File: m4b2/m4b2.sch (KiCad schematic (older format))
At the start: 40 parts, among them P10 MicroD-37Pins, U1 MC306, U10 MC308, U11 MC306, U12 MC311, U13 MC309, U14 MC306, U15 MC308, U16 MC306, U17 MC311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

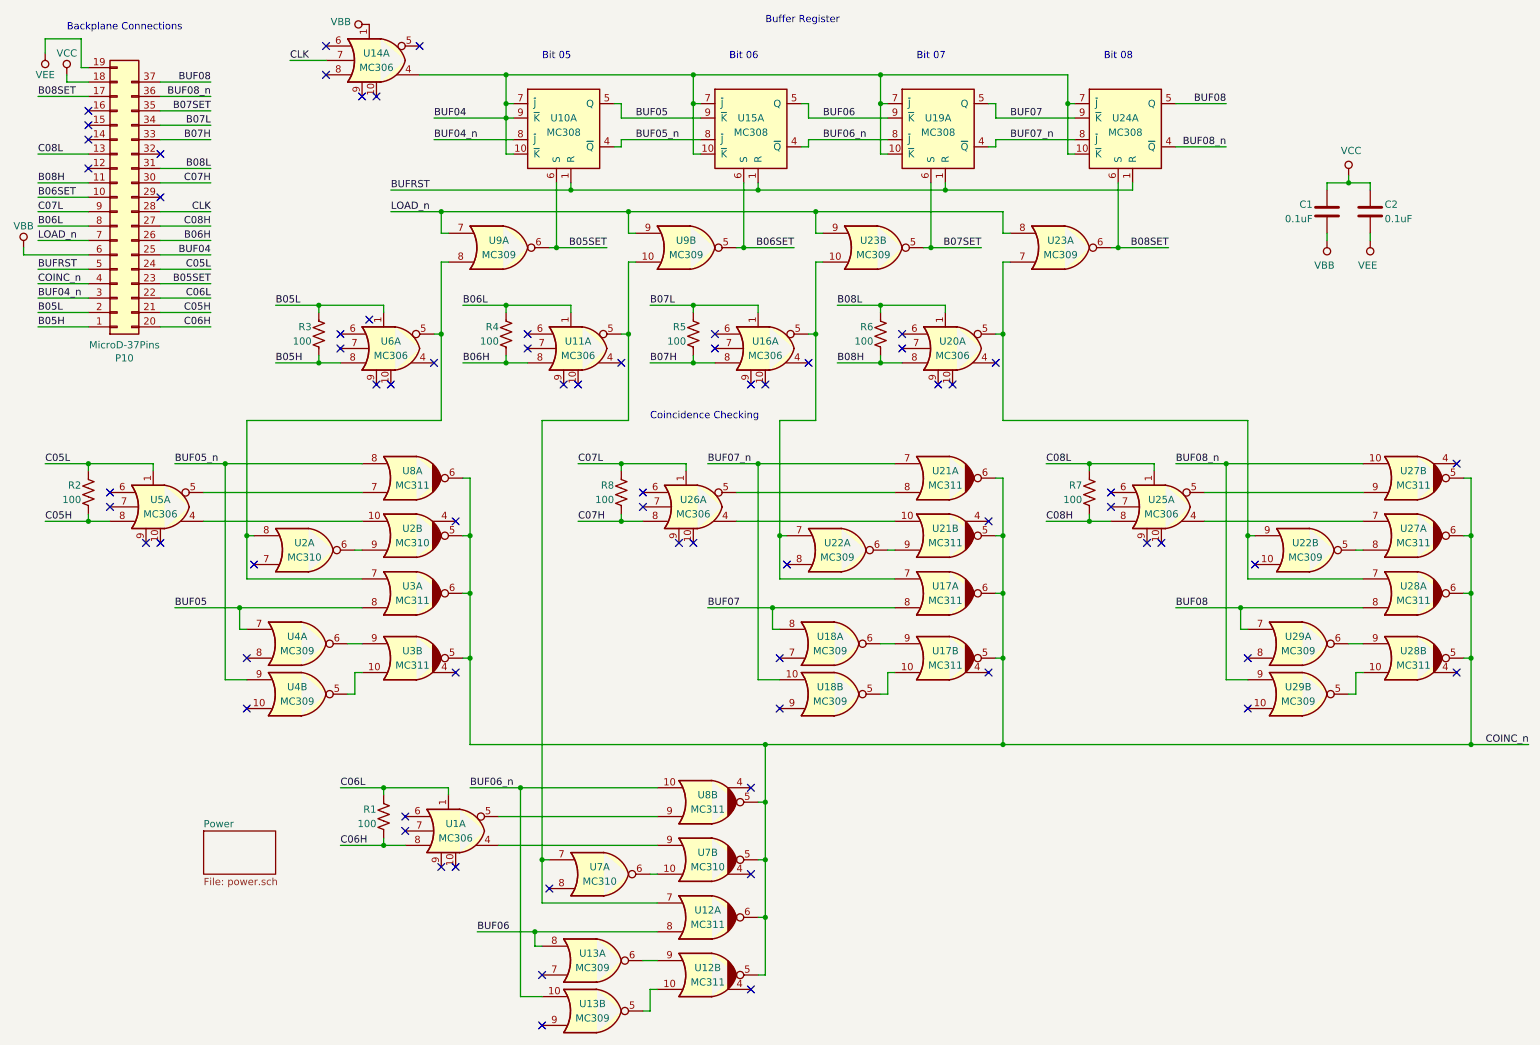
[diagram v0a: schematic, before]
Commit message: Added a schematic for module 4 board 2, which has two small differences from the other three four-bit modules. Also fixed a pinout error on module 5 board 2.
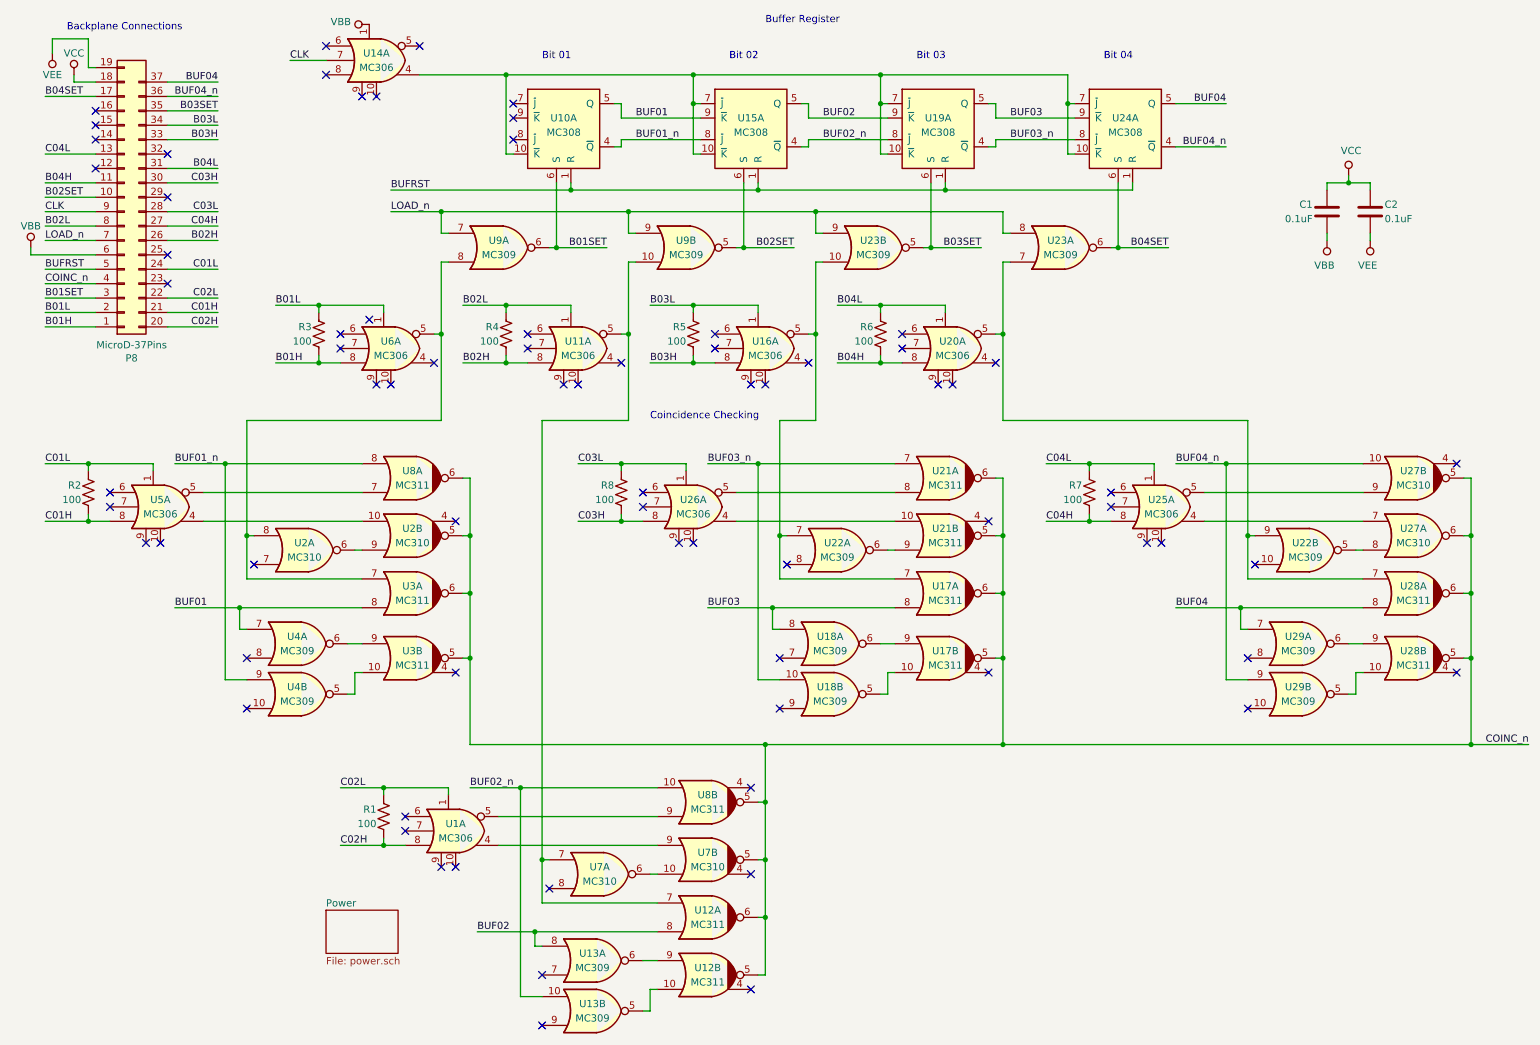
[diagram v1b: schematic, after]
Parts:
- removed P10: MicroD-37Pins, symbol gn_buffer:MicroD-37Pins
- removed U27: MC311, symbol gn_buffer:MC311
- added P8: MicroD-37Pins, symbol gn_buffer:MicroD-37Pins
- added U27: MC310, symbol gn_buffer:MC310
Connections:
- net BUF08 is gone; now on net BUF04: U24.5 (Q), U28.8, U29.7
- net BUF08_n is gone; now on net BUF04_n: U24.4 (~Q), U29.9
- net BUF04: now also P8.37 (Pin_37); no longer U10.10 (~K), U10.7 (~J), U10.9 (~K), U14.4, U15.10 (~K), U15.7 (~J), U19.10 (~K), U19.7 (~J), U24.10 (~K), U24.7 (~J)
- net BUF04_n: now also P8.36 (Pin_36), U27.10; no longer U10.8 (~J)
- net BUFRST: now also P8.5 (Pin_5)
- net CLK: now also P8.9 (Pin_9)
- net COINC_n: now also P8.4 (Pin_4), U27.5, U27.6
- net LOAD_n: now also P8.7 (Pin_7)
- net VBB: now also P8.6 (Pin_6)
- net VCC: now also P8.18 (Pin_18)
- net VEE: now also P8.19 (Pin_19)
- net at U25.4: now also U27.7
- net at U25.5: now also U27.9
- net at U22.5: now also U27.8
- net B05H renamed B01H
- net B01H: now also P8.1 (Pin_1)
- net B05L renamed B01L
- net B01L: now also P8.2 (Pin_2)
- net B05SET renamed B01SET
- net B01SET: now also P8.3 (Pin_3)
- net B06H renamed B02H
- net B02H: now also P8.26 (Pin_26)
- net B06L renamed B02L
- net B02L: now also P8.8 (Pin_8)
- net B06SET renamed B02SET
- net B02SET: now also P8.10 (Pin_10)
- net B07H renamed B03H
- net B03H: now also P8.33 (Pin_33)
- net B07L renamed B03L
- net B03L: now also P8.34 (Pin_34)
- net B07SET renamed B03SET
- net B03SET: now also P8.35 (Pin_35)
- net B08H renamed B04H
- net B04H: now also P8.11 (Pin_11)
- net B08L renamed B04L
- net B04L: now also P8.31 (Pin_31)
- net B08SET renamed B04SET
- net B04SET: now also P8.17 (Pin_17)
- net BUF05 renamed BUF01
- net BUF05_n renamed BUF01_n
- net BUF06 renamed BUF02
- net BUF06_n renamed BUF02_n
- net BUF07 renamed BUF03
- net BUF07_n renamed BUF03_n
- net C05H renamed C01H
- net C01H: now also P8.21 (Pin_21)
- net C05L renamed C01L
- net C01L: now also P8.24 (Pin_24)
- net C06H renamed C02H
- net C02H: now also P8.20 (Pin_20)
- net C06L renamed C02L
- net C02L: now also P8.22 (Pin_22)
- net C07H renamed C03H
- net C03H: now also P8.30 (Pin_30)
- net C07L renamed C03L
- net C03L: now also P8.28 (Pin_28)
- net C08H renamed C04H
- net C04H: now also P8.27 (Pin_27)
- net C08L renamed C04L
- net C04L: now also P8.13 (Pin_13)
- new net: U10.10 (~K), U14.4, U15.10 (~K), U15.7 (~J), U19.10 (~K), U19.7 (~J), U24.10 (~K), U24.7 (~J)
- no-connect marks 69 -> 74
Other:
- note added: "Bit 01"
- note added: "Bit 02"
- note added: "Bit 03"
- note added: "Bit 04"
- note removed: "Bit 05"
- note removed: "Bit 06"
- note removed: "Bit 07"
- note removed: "Bit 08"
